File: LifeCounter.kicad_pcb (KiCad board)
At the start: 2 copper layers, 100 x 74.8 mm, 210 parts, among them J201 USBC, J301 Debug, Q201 DO2308S, Q202 DO2309A, Q203 DO2309A, Q601 DO2309A, Q602 DO2309A, Q603 DO2309A, Q604 DO2309A, Q605 DO2309A, Q606 DO2309A, Q607 DO2309A, Q608 DO2309A, Q609 DO2308S, Q610 DO2308S, Q611 DO2308S, Q612 DO2308S, Q701 DO2309A, Q702 DO2309A, Q703 DO2309A, Q704 DO2309A, Q705 DO2309A, Q706 DO2309A, Q707 DO2309A, Q708 DO2309A, Q709 DO2308S, Q710 DO2308S, Q711 DO2308S, Q712 DO2308S, Q801 DO2308S, SW201 PWR_ON, SW301 RST, SW401 RotaryEncoder_Switch_MP, SW501 RotaryEncoder_Switch_MP, U201 TPS630701RNMR, U202 BQ24090DGQ, U203 BQ27441-G1, U301 STM32C031K6Tx, U401 74LVC3G14, U501 74LVC3G14, U601 74HC595, U603 CC56-12GWA, U604 74HC595, U701 74HC595, U703 CC56-12GWA, U704 74HC595

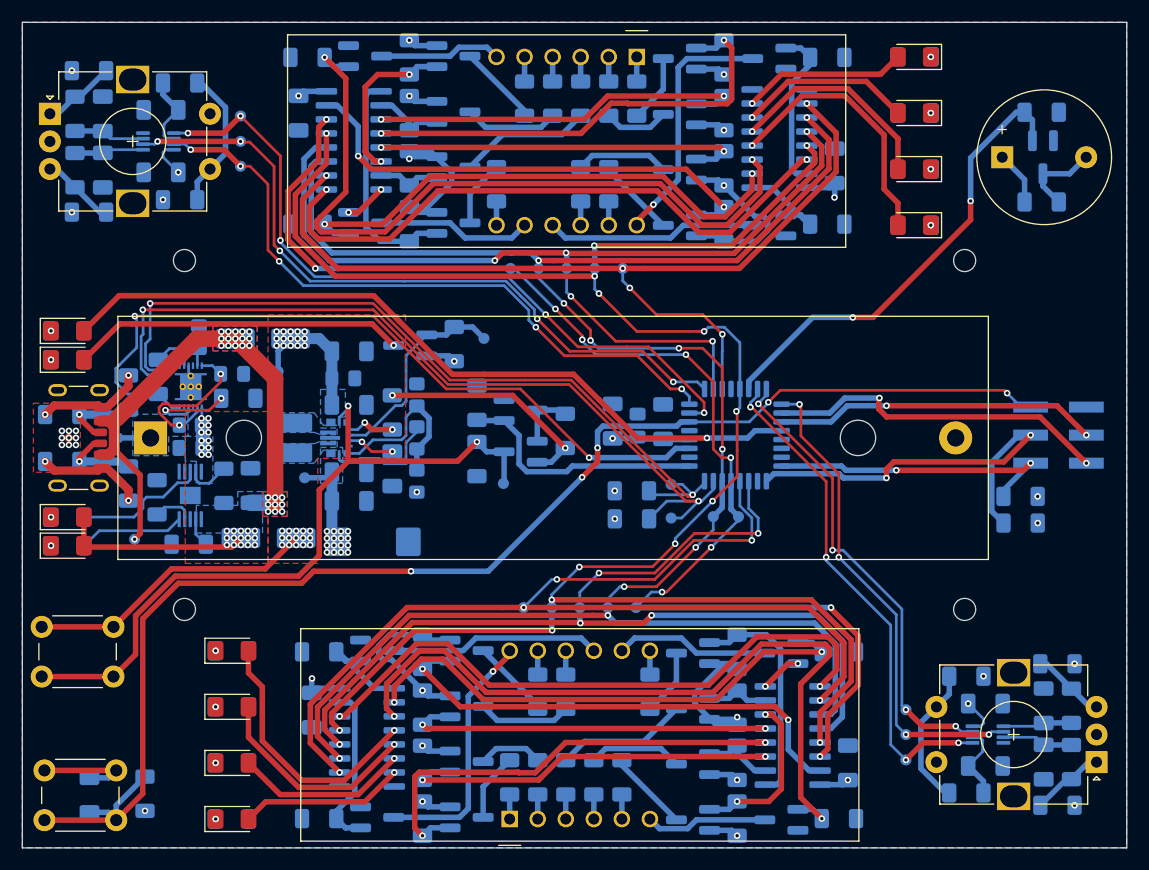
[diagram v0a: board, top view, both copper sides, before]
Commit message: Rounded PCB corners
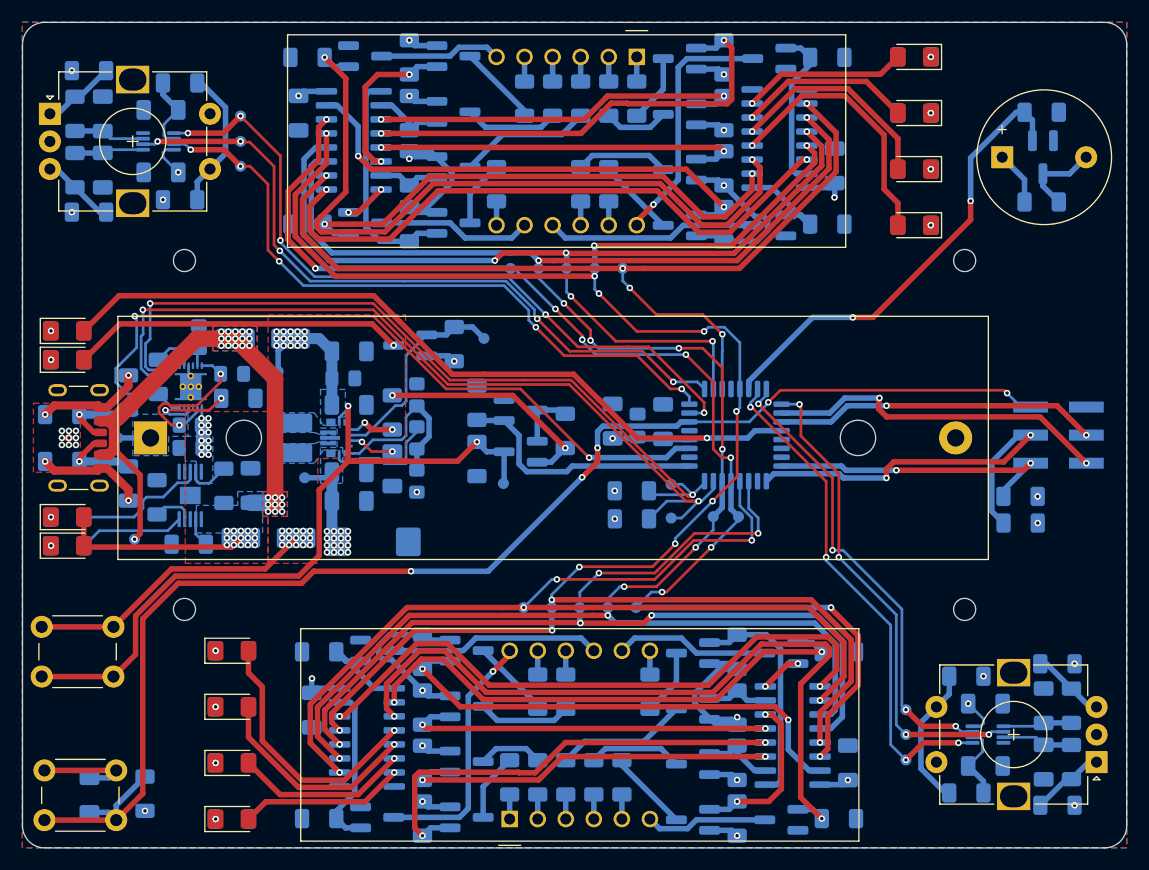
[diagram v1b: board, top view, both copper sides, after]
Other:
- outline, holes or cut-outs redrawn
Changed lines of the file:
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@@
 		(embedded_fonts no)
 	)
-	(gr_rect
-		(start 104 51.263375)
-		(end 204 126.013375)
+	(gr_arc
+		(start 202 51.263375)
+		(mid 203.414213 51.849161)
+		(end 204 53.263374)
+		(stroke
+			(width 0.05)
+			(type solid)
+		)
+		(layer "Edge.Cuts")
+	)
+	(gr_line
+		(start 204 53.263374)
+		(end 204 124.013375)
 		(stroke
 			(width 0.05)
 			(type default)
 		)
-		(fill no)
 		(layer "Edge.Cuts")
 	)
+	(gr_line
+		(start 201.990001 126.013375)
+		(end 106.013 126.013375)
+		(stroke
+			(width 0.05)
+			(type solid)
+		)
+		(layer "Edge.Cuts")
+	)
+	(gr_arc
+		(start 104.013 53.263375)
+		(mid 104.598786 51.849161)
+		(end 106.013 51.263375)
+		(stroke
+			(width 0.05)
+			(type solid)
+		)
+		(layer "Edge.Cuts")
+	)
+	(gr_line
+		(start 104.013 124.013376)
+		(end 104.013 53.2634)
+		(stroke
+			(width 0.05)
+			(type solid)
+		)
+		(layer "Edge.Cuts")
+	)
+	(gr_arc
+		(start 203.999999 124.013375)
+		(mid 203.414213 125.427588)
+		(end 202 126.013375)
+		(stroke
+			(width 0.05)
+			(type solid)
+		)
+		(layer "Edge.Cuts")
+	)
+	(gr_line
+		(start 106.013 51.263375)
+		(end 202 51.2634)
+		(stroke
+			(width 0.05)
+			(type solid)
+		)
+		(layer "Edge.Cuts")
+	)
+	(gr_arc
+		(start 106.013 126.013375)
+		(mid 104.598786 125.42759)
+		(end 104.013 124.013376)
+		(stroke
+			(width 0.05)
+			(type solid)
+		)
+		(layer "Edge.Cuts")
+	)

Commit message: Add version to silkscreen
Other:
- board text added: "Life Counter V${VERSION}"
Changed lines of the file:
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@@
 		)
 	)
+	(property "VERSION" "01.00")
 	(net 0 "")
 	(net 1 "Net-(BT201-+)")
@@
 		(layer "Edge.Cuts")
 	)
+	(gr_text "Life Counter\nV${VERSION}"
+		(at 197.612 89.027 90)
+		(layer "F.SilkS")
+		(effects
+			(font
+				(size 1.5 1.5)
+				(thickness 0.3)
+				(bold yes)
+			)
+		)
+	)
 	(segment
